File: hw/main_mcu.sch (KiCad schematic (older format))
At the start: 12 parts, among them J4 SWD_01X04, U5 STM32F405RGTx

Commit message: finished schematic
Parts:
- removed C11, C14, C17: 100n, symbol Device:C
- removed R11, R12: 10k, symbol Device:R
- added C2, C5, C8: 100n, symbol Device:C
- added J1: UART_01X03, Connector_PinHeader_2.54mm:PinHeader_1x03_P2.54mm_Vertical, symbol KLIB_Connector_Prog:UART_01X03
- added R1, R2: 10k, symbol Device:R
- renumbered C10 to C1, C12 to C3, C13 to C4, C15 to C6, C16 to C7, J4 to J2, U5 to U1
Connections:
- net USB_UART_CTS is gone; now on net ~RF_ENABLE: U1.44 (ADC1_EXTI11/ADC2_EXTI11/ADC3_EXTI11/CAN1_RX/TIM1_CH4/USART1_CTS/USB_OTG_FS_DM/PA11)
- net USB_UART_RTS is gone; now on net ~RF_CONFIG: U1.45 (CAN1_TX/TIM1_ETR/USART1_RTS/USB_OTG_FS_DP/PA12)
- net USB_UART_RX is gone; now on net RF_UART_RX: U1.43 (TIM1_CH3/USART1_RX/USB_OTG_FS_ID/PA10)
- net USB_UART_TX is gone; now on net RF_UART_TX: U1.42 (DAC_EXTI9/I2C3_SMBA/TIM1_CH2/USART1_TX/USB_OTG_FS_VBUS/PA9)
- net +3V3: now also C5.1, C8.1, R2.1
- net DEBUG_UART_RX: now also U1.15 (ADC1_IN1/ADC2_IN1/ADC3_IN1/TIM2_CH2/TIM5_CH2/UART4_RX/USART2_RTS/PA1), J1.2 (RX); no longer U1.30 (ADC1_EXTI11/ADC2_EXTI11/ADC3_EXTI11/I2C2_SDA/TIM2_CH4/USART3_RX/USB_OTG_HS_ULPI_D4/PB11)
- net DEBUG_UART_TX: now also U1.14 (ADC1_IN0/ADC2_IN0/ADC3_IN0/SYS_WKUP/TIM2_CH1/TIM2_ETR/TIM5_CH1/TIM8_ETR/UART4_TX/USART2_CTS/PA0), J1.3 (TX); no longer U1.29 (I2C2_SCL/I2S2_CK/SPI2_SCK/TIM2_CH3/USART3_TX/USB_OTG_HS_ULPI_D3/PB10)
- net GND: now also C2.2, C5.2, C8.2, J1.1 (GND), R1.1
- net RF_UART_RX: no longer U1.17 (ADC1_IN3/ADC2_IN3/ADC3_IN3/TIM2_CH4/TIM5_CH4/TIM9_CH2/USART2_RX/USB_OTG_HS_ULPI_D0/PA3)
- net RF_UART_TX: no longer U1.16 (ADC1_IN2/ADC2_IN2/ADC3_IN2/TIM2_CH3/TIM5_CH3/TIM9_CH1/USART2_TX/PA2)
- net ~RF_CONFIG: no longer U1.14 (ADC1_IN0/ADC2_IN0/ADC3_IN0/SYS_WKUP/TIM2_CH1/TIM2_ETR/TIM5_CH1/TIM8_ETR/UART4_TX/USART2_CTS/PA0)
- net ~RF_ENABLE: no longer U1.15 (ADC1_IN1/ADC2_IN1/ADC3_IN1/TIM2_CH2/TIM5_CH2/UART4_RX/USART2_RTS/PA1)
- net ~RST: now also R2.2
- net A6: now reaches U1.10 (PC2/ADC1_IN12/ADC2_IN12/ADC3_IN12/I2S2_ext_SD/SPI2_MISO/USB_OTG_HS_ULPI_DIR)
- net A7: now reaches U1.11 (PC3/ADC1_IN13/ADC2_IN13/ADC3_IN13/I2S2_SD/SPI2_MOSI/USB_OTG_HS_ULPI_NXT)
- net ~BTN: now reaches U1.2 (PC13/ANTI_TAMP/RTC_AF1)
- net PWM_R: now reaches U1.22 (ADC1_IN6/ADC2_IN6/SPI1_MISO/TIM13_CH1/TIM1_BKIN/TIM3_CH1/TIM8_BKIN/PA6)
- net PWM_G: now reaches U1.23 (ADC1_IN7/ADC2_IN7/SPI1_MOSI/TIM14_CH1/TIM1_CH1N/TIM3_CH2/TIM8_CH1N/PA7)
- net PWM_B: now reaches U1.26 (ADC1_IN8/ADC2_IN8/TIM1_CH2N/TIM3_CH3/TIM8_CH2N/USB_OTG_HS_ULPI_D1/PB0)
- net A0: now reaches U1.3 (PC14/RCC_OSC32_IN)
- net SOUND_UART_TX: now reaches U1.37 (PC6/I2S2_MCK/SDIO_D6/TIM3_CH1/TIM8_CH1/USART6_TX)
- net SOUND_UART_RX: now reaches U1.38 (PC7/I2S3_MCK/SDIO_D7/TIM3_CH2/TIM8_CH2/USART6_RX)
- net SOUND_SEL0: now reaches U1.39 (PC8/SDIO_D0/TIM3_CH3/TIM8_CH3/USART6_CK)
- net A1: now reaches U1.4 (PC15/ADC1_EXTI15/ADC2_EXTI15/ADC3_EXTI15/RCC_OSC32_OUT)
- net SOUND_SEL1: now reaches U1.40 (PC9/DAC_EXTI9/I2C3_SDA/I2S_CKIN/RCC_MCO_2/SDIO_D1/TIM3_CH4/TIM8_CH4)
- net IR_RX: now reaches U1.41 (I2C3_SCL/RCC_MCO_1/TIM1_CH1/USART1_CK/USB_OTG_FS_SOF/PA8)
- net at U1.47 (VCAP_2): now also C2.1
- net A2: now reaches U1.5 (PH0/RCC_OSC_IN)
- net LCD_UART_TX: now reaches U1.51 (PC10/I2S3_CK/SDIO_D2/SPI3_SCK/UART4_TX/USART3_TX)
- net LCD_UART_RX: now reaches U1.52 (PC11/ADC1_EXTI11/ADC2_EXTI11/ADC3_EXTI11/I2S3_ext_SD/SDIO_D3/SPI3_MISO/UART4_RX/USART3_RX)
- net ~LCD_RST: now reaches U1.53 (PC12/I2S3_SD/SDIO_CK/SPI3_MOSI/UART5_TX/USART3_CK)
- net ~INT: now reaches U1.56 (I2S3_ext_SD/SPI1_MISO/SPI3_MISO/SYS_JTRST/TIM3_CH1/PB4)
- net ~AL: now reaches U1.57 (CAN2_RX/I2C1_SMBA/I2S3_SD/SPI1_MOSI/SPI3_MOSI/TIM3_CH2/USB_OTG_HS_ULPI_D7/PB5)
- net SCL: now reaches U1.58 (CAN2_TX/I2C1_SCL/TIM4_CH1/USART1_TX/PB6)
- net SDA: now reaches U1.59 (I2C1_SDA/TIM4_CH2/USART1_RX/PB7)
- net A3: now reaches U1.6 (PH1/RCC_OSC_OUT)
- net at U1.60 (BOOT0): now also R1.2
- net A4: now reaches U1.8 (PC0/ADC1_IN10/ADC2_IN10/ADC3_IN10/USB_OTG_HS_ULPI_STP)
- net A5: now reaches U1.9 (PC1/ADC1_IN11/ADC2_IN11/ADC3_IN11)
- new net GUN_UART_RX: U1.17 (ADC1_IN3/ADC2_IN3/ADC3_IN3/TIM2_CH4/TIM5_CH4/TIM9_CH2/USART2_RX/USB_OTG_HS_ULPI_D0/PA3)
- new net GUN_UART_TX: U1.16 (ADC1_IN2/ADC2_IN2/ADC3_IN2/TIM2_CH3/TIM5_CH3/TIM9_CH1/USART2_TX/PA2)
- no-connect marks 31 -> 17

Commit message: updated schematic added footptints
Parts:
- C1, C2, C3, C4, C5, C6, C7, C8: footprint (none) -> Capacitor_SMD:C_0805_2012Metric
- R1, R2: footprint (none) -> Resistor_SMD:R_0805_2012Metric
- U1: footprint LQFP64 -> Package_QFP:TQFP-64_10x10mm_P0.5mm
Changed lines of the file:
@@
 F 0 "U1" H 1650 5850 50  0000 L CNN
 F 1 "STM32F405RGTx" H 1650 5750 50  0000 L CNN
-F 2 "LQFP64" H 10050 5625 50  0001 R TNN
+F 2 "Package_QFP:TQFP-64_10x10mm_P0.5mm" H 10050 5625 50  0001 R TNN
 F 3 "http://www.st.com/st-web-ui/static/active/en/resource/technical/document/datasheet/DM00037051.pdf" H 5850 3750 50  0001 C CNN
 	1    5850 3750
@@
 F 0 "R2" H 1170 1996 50  0000 L CNN
 F 1 "10k" H 1170 1905 50  0000 L CNN
-F 2 "" V 1030 1950 50  0001 C CNN
+F 2 "Resistor_SMD:R_0805_2012Metric" V 1030 1950 50  0001 C CNN
 F 3 "~" H 1100 1950 50  0001 C CNN
 	1    1100 1950
@@
 F 0 "R1" H 820 1996 50  0000 L CNN
 F 1 "10k" H 820 1905 50  0000 L CNN
-F 2 "" V 680 1950 50  0001 C CNN
+F 2 "Resistor_SMD:R_0805_2012Metric" V 680 1950 50  0001 C CNN
 F 3 "~" H 750 1950 50  0001 C CNN
 	1    750  1950
@@
 F 0 "C1" H 865 2996 50  0000 L CNN
 F 1 "100n" H 865 2905 50  0000 L CNN
-F 2 "" H 788 2800 50  0001 C CNN
+F 2 "Capacitor_SMD:C_0805_2012Metric" H 788 2800 50  0001 C CNN
 F 3 "~" H 750 2950 50  0001 C CNN
 	1    750  2950
@@
 F 0 "C2" H 1365 2996 50  0000 L CNN
 F 1 "100n" H 1365 2905 50  0000 L CNN
-F 2 "" H 1288 2800 50  0001 C CNN
+F 2 "Capacitor_SMD:C_0805_2012Metric" H 1288 2800 50  0001 C CNN
 F 3 "~" H 1250 2950 50  0001 C CNN
 	1    1250 2950
@@
 F 0 "C4" H 7865 1196 50  0000 L CNN
 F 1 "100n" H 7865 1105 50  0000 L CNN
-F 2 "" H 7788 1000 50  0001 C CNN
+F 2 "Capacitor_SMD:C_0805_2012Metric" H 7788 1000 50  0001 C CNN
 F 3 "~" H 7750 1150 50  0001 C CNN
 	1    7750 1150
@@
 F 0 "C5" H 8315 1196 50  0000 L CNN
 F 1 "100n" H 8315 1105 50  0000 L CNN
-F 2 "" H 8238 1000 50  0001 C CNN
+F 2 "Capacitor_SMD:C_0805_2012Metric" H 8238 1000 50  0001 C CNN
 F 3 "~" H 8200 1150 50  0001 C CNN
 	1    8200 1150
@@
 F 0 "C6" H 8765 1196 50  0000 L CNN
 F 1 "100n" H 8765 1105 50  0000 L CNN
-F 2 "" H 8688 1000 50  0001 C CNN
+F 2 "Capacitor_SMD:C_0805_2012Metric" H 8688 1000 50  0001 C CNN
 F 3 "~" H 8650 1150 50  0001 C CNN
 	1    8650 1150
@@
 F 0 "C7" H 9215 1196 50  0000 L CNN
 F 1 "100n" H 9215 1105 50  0000 L CNN
-F 2 "" H 9138 1000 50  0001 C CNN
+F 2 "Capacitor_SMD:C_0805_2012Metric" H 9138 1000 50  0001 C CNN
 F 3 "~" H 9100 1150 50  0001 C CNN
 	1    9100 1150
@@
 F 0 "C8" H 9665 1196 50  0000 L CNN
 F 1 "100n" H 9665 1105 50  0000 L CNN
-F 2 "" H 9588 1000 50  0001 C CNN
+F 2 "Capacitor_SMD:C_0805_2012Metric" H 9588 1000 50  0001 C CNN
 F 3 "~" H 9550 1150 50  0001 C CNN
 	1    9550 1150
@@
 F 0 "C3" H 7415 1196 50  0000 L CNN
 F 1 "100n" H 7415 1105 50  0000 L CNN
-F 2 "" H 7338 1000 50  0001 C CNN
+F 2 "Capacitor_SMD:C_0805_2012Metric" H 7338 1000 50  0001 C CNN
 F 3 "~" H 7300 1150 50  0001 C CNN
 	1    7300 1150

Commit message: placement component to pcb
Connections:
- net A0: now also U1.11 (PC3/ADC1_IN13/ADC2_IN13/ADC3_IN13/I2S2_SD/SPI2_MOSI/USB_OTG_HS_ULPI_NXT); no longer U1.3 (PC14/RCC_OSC32_IN)
- net A1: now also U1.10 (PC2/ADC1_IN12/ADC2_IN12/ADC3_IN12/I2S2_ext_SD/SPI2_MISO/USB_OTG_HS_ULPI_DIR); no longer U1.4 (PC15/ADC1_EXTI15/ADC2_EXTI15/ADC3_EXTI15/RCC_OSC32_OUT)
- net A2: now also U1.9 (PC1/ADC1_IN11/ADC2_IN11/ADC3_IN11); no longer U1.5 (PH0/RCC_OSC_IN)
- net A3: now also U1.8 (PC0/ADC1_IN10/ADC2_IN10/ADC3_IN10/USB_OTG_HS_ULPI_STP); no longer U1.6 (PH1/RCC_OSC_OUT)
- net A4: now also U1.6 (PH1/RCC_OSC_OUT); no longer U1.8 (PC0/ADC1_IN10/ADC2_IN10/ADC3_IN10/USB_OTG_HS_ULPI_STP)
- net A5: now also U1.5 (PH0/RCC_OSC_IN); no longer U1.9 (PC1/ADC1_IN11/ADC2_IN11/ADC3_IN11)
- net A6: now also U1.4 (PC15/ADC1_EXTI15/ADC2_EXTI15/ADC3_EXTI15/RCC_OSC32_OUT); no longer U1.10 (PC2/ADC1_IN12/ADC2_IN12/ADC3_IN12/I2S2_ext_SD/SPI2_MISO/USB_OTG_HS_ULPI_DIR)
- net A7: now also U1.3 (PC14/RCC_OSC32_IN); no longer U1.11 (PC3/ADC1_IN13/ADC2_IN13/ADC3_IN13/I2S2_SD/SPI2_MOSI/USB_OTG_HS_ULPI_NXT)
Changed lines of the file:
@@
-$EndComp
-$Comp
-L Device:C C8
-U 1 1 5AD7FB38
-P 9550 1150
-F 0 "C8" H 9665 1196 50  0000 L CNN
-F 1 "100n" H 9665 1105 50  0000 L CNN
-F 2 "Capacitor_SMD:C_0805_2012Metric" H 9588 1000 50  0001 C CNN
-F 3 "~" H 9550 1150 50  0001 C CNN
-	1    9550 1150
-	1    0    0    -1
 $EndComp
 $Comp
@@
 	7300 1350 7750 1350
 Wire Wire Line
-	9550 1300 9550 1350
-Wire Wire Line
 	9100 1300 9100 1350
-Connection ~ 9100 1350
-Wire Wire Line
-	9100 1350 9550 1350
 Wire Wire Line
 	8650 1300 8650 1350
@@
 Connection ~ 8200 1350
 Wire Wire Line
-	8200 1350 8450 1350
-Wire Wire Line
 	7750 1300 7750 1350
 Connection ~ 7750 1350
@@
 Connection ~ 8200 950
 Wire Wire Line
-	8200 950  8450 950
-Wire Wire Line
 	8650 1000 8650 950
 Connection ~ 8650 950
@@
 Wire Wire Line
 	9100 1000 9100 950
-Connection ~ 9100 950
-Wire Wire Line
-	9100 950  9550 950
-Wire Wire Line
-	9550 1000 9550 950
 $Comp
 L KLIB_Power:+3V3 #PWR09
@@
 	1    0    0    -1
 $EndComp
-Wire Wire Line
-	8450 1400 8450 1350
-Connection ~ 8450 1350
-Wire Wire Line
-	8450 1350 8650 1350
-Wire Wire Line
-	8450 900  8450 950
-Connection ~ 8450 950
-Wire Wire Line
-	8450 950  8650 950
 $Comp
 L KLIB_Power:PWR_FLAG #FLG01
@@
 	1550 5250 1300 5250
 Text HLabel 1300 5250 0    50   Input ~ 0
-A0
+A7
 Wire Wire Line
 	1550 5350 1300 5350
 Text HLabel 1300 5350 0    50   Input ~ 0
-A1
+A6
 Wire Wire Line
 	1550 3350 1300 3350
 Text HLabel 1300 3350 0    50   Input ~ 0
-A2
+A5
 Wire Wire Line
 	1550 3450 1300 3450
 Text HLabel 1300 3450 0    50   Input ~ 0
-A3
+A4
 NoConn ~ 1550 4250
 NoConn ~ 1550 4350
@@
 	1550 3850 1300 3850
 Text HLabel 1300 3850 0    50   Input ~ 0
-A4
+A3
 Wire Wire Line
 	1550 3950 1300 3950
 Text HLabel 1300 3950 0    50   Input ~ 0
-A5
+A2
 Wire Wire Line
 	1550 4050 1300 4050
 Text HLabel 1300 4050 0    50   Input ~ 0
-A6
+A1
 Wire Wire Line
 	1550 4150 1300 4150
 Text HLabel 1300 4150 0    50   Input ~ 0
-A7
+A0
 $Comp
 L KLIB_Connector_Prog:UART_01X03 J1
@@
 NoConn ~ 10150 4850
 NoConn ~ 10150 4950
+Wire Wire Line
+	8450 950  8650 950
+Wire Wire Line
+	8200 950  8450 950
+Connection ~ 8450 950
+Wire Wire Line
+	8450 900  8450 950
+Wire Wire Line
+	8450 1350 8650 1350
+Wire Wire Line
+	8200 1350 8450 1350
+Connection ~ 8450 1350
+Wire Wire Line
+	8450 1400 8450 1350
+Connection ~ 9100 1350
+Wire Wire Line
+	9100 1350 9550 1350
+Wire Wire Line
+	9550 1300 9550 1350
+Connection ~ 9100 950
+Wire Wire Line
+	9100 950  9550 950
+Wire Wire Line
+	9550 1000 9550 950
+$Comp
+L Device:C C8
+U 1 1 5AD7FB38
+P 9550 1150
+F 0 "C8" H 9665 1196 50  0000 L CNN
+F 1 "100n" H 9665 1105 50  0000 L CNN
+F 2 "Capacitor_SMD:C_0805_2012Metric" H 9588 1000 50  0001 C CNN
+F 3 "~" H 9550 1150 50  0001 C CNN
+	1    9550 1150
+	1    0    0    -1
+$EndComp
 $EndSCHEMATC

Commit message: updated pcb
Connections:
- net PWM_B: now also U1.22 (ADC1_IN6/ADC2_IN6/SPI1_MISO/TIM13_CH1/TIM1_BKIN/TIM3_CH1/TIM8_BKIN/PA6); no longer U1.26 (ADC1_IN8/ADC2_IN8/TIM1_CH2N/TIM3_CH3/TIM8_CH2N/USB_OTG_HS_ULPI_D1/PB0)
- net PWM_R: now also U1.26 (ADC1_IN8/ADC2_IN8/TIM1_CH2N/TIM3_CH3/TIM8_CH2N/USB_OTG_HS_ULPI_D1/PB0); no longer U1.22 (ADC1_IN6/ADC2_IN6/SPI1_MISO/TIM13_CH1/TIM1_BKIN/TIM3_CH1/TIM8_BKIN/PA6)
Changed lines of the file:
@@
 Wire Wire Line
 	10150 2750 10400 2750
-Text HLabel 10400 2750 2    50   Output ~ 0
+Text HLabel 10400 3850 2    50   Output ~ 0
 PWM_R
 Text HLabel 10400 2850 2    50   Output ~ 0
@@
 Wire Wire Line
 	10150 2850 10400 2850
-Text HLabel 10400 3850 2    50   Output ~ 0
+Text HLabel 10400 2750 2    50   Output ~ 0
 PWM_B
 Wire Wire Line

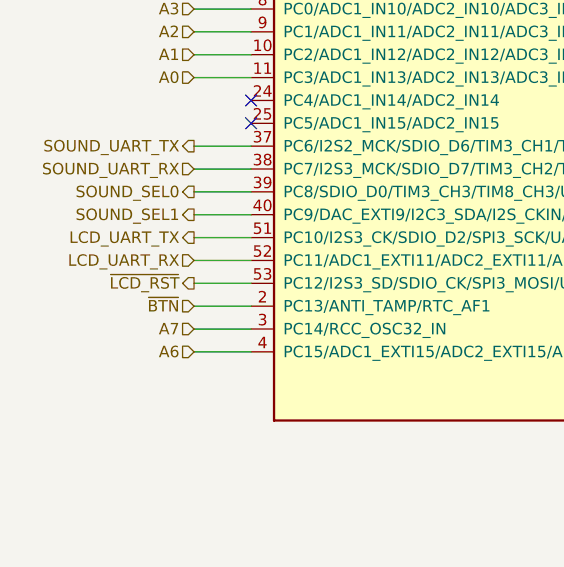
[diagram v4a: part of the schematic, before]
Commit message: removed LCD RST signal
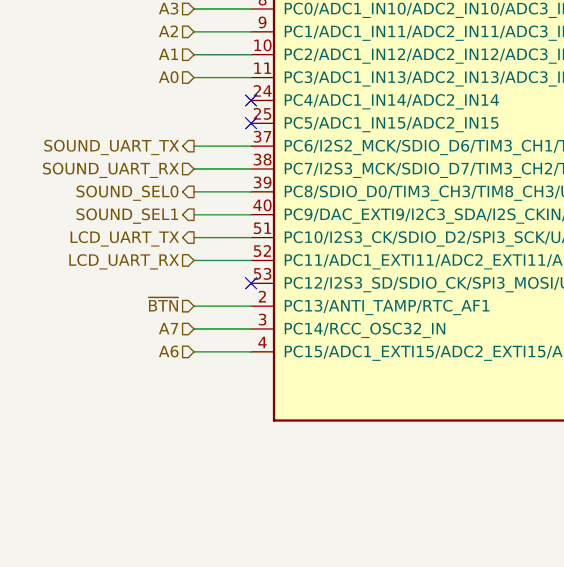
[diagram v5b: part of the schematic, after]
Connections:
- net ~LCD_RST: no longer names the net of U1.53 (PC12/I2S3_SD/SDIO_CK/SPI3_MOSI/UART5_TX/USART3_CK)
- no-connect marks 17 -> 18
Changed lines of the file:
@@
 Text HLabel 1300 4750 0    50   Output ~ 0
 SOUND_SEL1
-Text HLabel 1300 5050 0    50   Output ~ 0
-~LCD_RST
-Wire Wire Line
-	1550 5050 1300 5050
 Wire Wire Line
 	10150 4450 10400 4450
@@
 	1    0    0    -1
 $EndComp
+NoConn ~ 1550 5050
 $EndSCHEMATC
